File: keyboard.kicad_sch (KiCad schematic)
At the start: 207 parts, among them J2 USB_C_Receptacle_USB2.0_16P, J4 Conn_01x05, SW1 SW_Push, SW2 SW_Push, U1 RP2040, U2 XC6206PxxxMR, U3 W25Q128JVS, Y1 Crystal_GND24

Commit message: add logic level shifter to top sheet
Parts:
- added C101: 100n, symbol Device:C
- added R85: 470, symbol Device:R
- added U85: 74AHCT1G125, symbol 74xGxx:74AHCT1G125
- renumbered C16 to C100, C2 to C85, C3 to C86, C11 to C87, C10 to C88, C9 to C89, C8 to C90, C7 to C91, C6 to C92, C5 to C93, C4 to C94, C1 to C95, C12 to C96, C13 to C97, C15 to C98, C14 to C99, J2 to J1, J4 to J2, R8 to R1, R11 to R3, R1 to R4, R10 to R5, R9 to R6, R3 to R8, R6 to R9, S30 to S1, S59 to S2, S61 to S3, S78 to S4
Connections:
- net +5V: now also C101.1, U85.5 (VCC)
- net GND: now also C101.2, U85.1, U85.3 (GND)
- new net: R85.1, U85.4
- new net LED_DATA: R85.2, U85.2
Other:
- added sheet LED_link (LED_link_sch.kicad_sch)
- note added: "Logic Level Shifter"

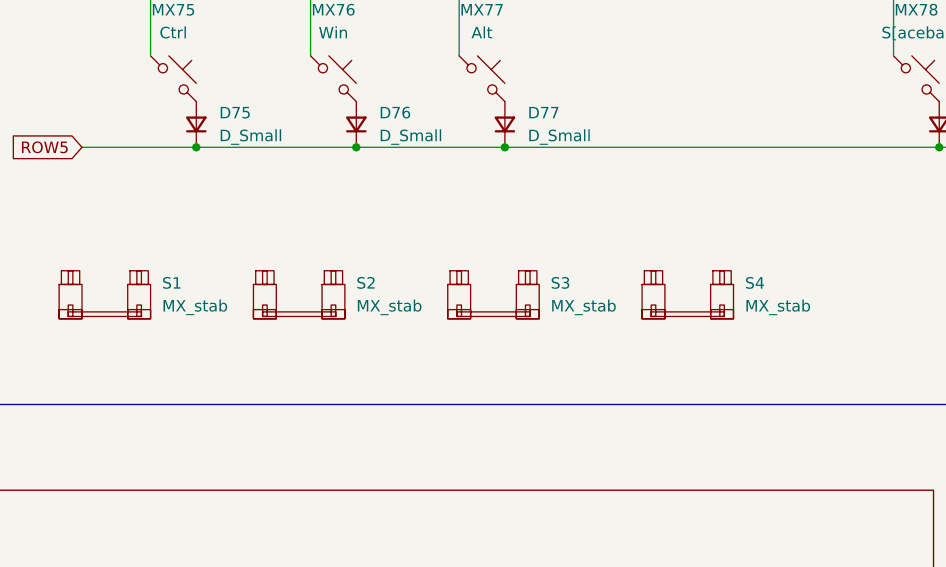
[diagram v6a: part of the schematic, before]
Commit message: flip mx switches, need to flip others as well
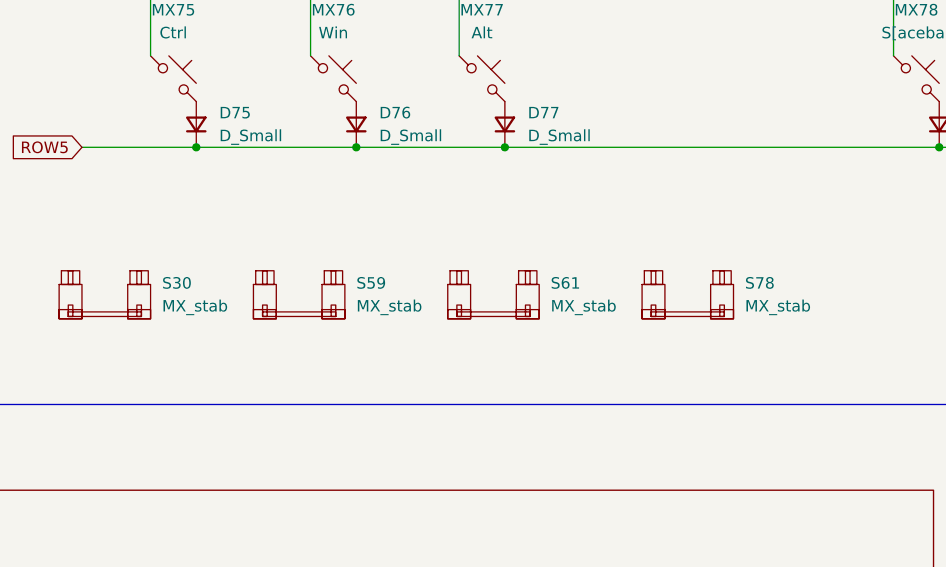
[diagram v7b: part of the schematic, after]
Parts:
- C100, C85, C86, C87, C88, C89, C90, C91, C92, C93, C94, C95, C98, C99: footprint Capacitor_SMD:C_0402_1005Metric -> Capacitor_SMD:C_0402_1005Metric_Pad0.74x0.62mm_HandSolder
- C101: footprint (none) -> Capacitor_SMD:C_0402_1005Metric_Pad0.74x0.62mm_HandSolder
- C96, C97: footprint Capacitor_SMD:C_0603_1608Metric -> Capacitor_SMD:C_0402_1005Metric_Pad0.74x0.62mm_HandSolder
- R85: footprint (none) -> Resistor_SMD:R_0402_1005Metric_Pad0.72x0.64mm_HandSolder
- U85: footprint (none) -> Package_TO_SOT_SMD:SOT-23-5_HandSoldering
- renumbered S1 to S30, S2 to S59, S3 to S61, S4 to S78
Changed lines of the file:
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@@
 			)
 		)
-		(property "Footprint" "Capacitor_SMD:C_0402_1005Metric"
+		(property "Footprint" "Capacitor_SMD:C_0402_1005Metric_Pad0.74x0.62mm_HandSolder"
 			(at 87.3252 34.29 0)
 			(hide yes)
@@
 		(dnp no)
 		(fields_autoplaced yes)
-		(property "Reference" "S4"
+		(property "Reference" "S78"
 			(at 323.85 162.4329 0)
 			(show_name no)
@@
 			(project "keyboard"
 				(path "/4d03a9a6-8b5c-48be-8b99-d5cd1aeff9bb"
-					(reference "S4")
+					(reference "S78")
 					(unit 1)
 				)
@@
 			)
 		)
-		(property "Footprint" "Capacitor_SMD:C_0603_1608Metric"
+		(property "Footprint" "Capacitor_SMD:C_0402_1005Metric_Pad0.74x0.62mm_HandSolder"
 			(at 88.5952 182.88 0)
 			(hide yes)
@@
 			)
 		)
-		(property "Footprint" "Capacitor_SMD:C_0402_1005Metric"
+		(property "Footprint" "Capacitor_SMD:C_0402_1005Metric_Pad0.74x0.62mm_HandSolder"
 			(at 149.5552 45.72 0)
 			(hide yes)
@@
 			)
 		)
-		(property "Footprint" ""
+		(property "Footprint" "Resistor_SMD:R_0402_1005Metric_Pad0.72x0.64mm_HandSolder"
 			(at 102.87 337.058 90)
 			(hide yes)
@@
 		(dnp no)
 		(fields_autoplaced yes)
-		(property "Reference" "S2"
+		(property "Reference" "S59"
 			(at 280.67 162.4329 0)
 			(show_name no)
@@
 			(project "keyboard"
 				(path "/4d03a9a6-8b5c-48be-8b99-d5cd1aeff9bb"
-					(reference "S2")
+					(reference "S59")
 					(unit 1)
 				)
@@
 			)
 		)
-		(property "Footprint" "Capacitor_SMD:C_0402_1005Metric"
+		(property "Footprint" "Capacitor_SMD:C_0402_1005Metric_Pad0.74x0.62mm_HandSolder"
 			(at 180.0352 241.3 0)
 			(hide yes)
@@
 			)
 		)
-		(property "Footprint" "Capacitor_SMD:C_0402_1005Metric"
+		(property "Footprint" "Capacitor_SMD:C_0402_1005Metric_Pad0.74x0.62mm_HandSolder"
 			(at 162.2552 33.02 0)
 			(hide yes)
@@
 			)
 		)
-		(property "Footprint" "Capacitor_SMD:C_0402_1005Metric"
+		(property "Footprint" "Capacitor_SMD:C_0402_1005Metric_Pad0.74x0.62mm_HandSolder"
 			(at 29.21 248.6152 0)
 			(hide yes)
@@
 		(dnp no)
 		(fields_autoplaced yes)
-		(property "Reference" "S1"
+		(property "Reference" "S30"
 			(at 259.08 162.4329 0)
 			(show_name no)
@@
 			(project "keyboard"
 				(path "/4d03a9a6-8b5c-48be-8b99-d5cd1aeff9bb"
-					(reference "S1")
+					(reference "S30")
 					(unit 1)
 				)
@@
 			)
 		)
-		(property "Footprint" "Capacitor_SMD:C_0402_1005Metric"
+		(property "Footprint" "Capacitor_SMD:C_0402_1005Metric_Pad0.74x0.62mm_HandSolder"
 			(at 149.5552 33.02 0)
 			(hide yes)
@@
 			)
 		)
-		(property "Footprint" "Capacitor_SMD:C_0603_1608Metric"
+		(property "Footprint" "Capacitor_SMD:C_0402_1005Metric_Pad0.74x0.62mm_HandSolder"
 			(at 125.4252 182.88 0)
 			(hide yes)
@@
 			)
 		)
-		(property "Footprint" ""
+		(property "Footprint" "Capacitor_SMD:C_0402_1005Metric_Pad0.74x0.62mm_HandSolder"
 			(at 41.6052 326.39 0)
 			(hide yes)
@@
 			)
 		)
-		(property "Footprint" "Capacitor_SMD:C_0402_1005Metric"
+		(property "Footprint" "Capacitor_SMD:C_0402_1005Metric_Pad0.74x0.62mm_HandSolder"
 			(at 61.9252 34.29 0)
 			(hide yes)
@@
 			)
 		)
-		(property "Footprint" "Capacitor_SMD:C_0402_1005Metric"
+		(property "Footprint" "Capacitor_SMD:C_0402_1005Metric_Pad0.74x0.62mm_HandSolder"
 			(at 49.2252 34.29 0)
 			(hide yes)
@@
 			)
 		)
-		(property "Footprint" "Capacitor_SMD:C_0402_1005Metric"
+		(property "Footprint" "Capacitor_SMD:C_0402_1005Metric_Pad0.74x0.62mm_HandSolder"
 			(at 35.2552 34.29 0)
 			(hide yes)
@@
 			)
 		)
-		(property "Footprint" "Capacitor_SMD:C_0402_1005Metric"
+		(property "Footprint" "Capacitor_SMD:C_0402_1005Metric_Pad0.74x0.62mm_HandSolder"
 			(at 36.83 233.9848 0)
 			(hide yes)
@@
 		(dnp no)
 		(fields_autoplaced yes)
-		(property "Reference" "S3"
+		(property "Reference" "S61"
 			(at 302.26 162.4329 0)
 			(show_name no)
@@
 			(project "keyboard"
 				(path "/4d03a9a6-8b5c-48be-8b99-d5cd1aeff9bb"
-					(reference "S3")
+					(reference "S61")
 					(unit 1)
 				)
@@
 			)
 		)
-		(property "Footprint" "Capacitor_SMD:C_0402_1005Metric"
+		(property "Footprint" "Capacitor_SMD:C_0402_1005Metric_Pad0.74x0.62mm_HandSolder"
 			(at 74.6252 34.29 0)
 			(hide yes)
@@
 			)
 		)
-		(property "Footprint" ""
+		(property "Footprint" "Package_TO_SOT_SMD:SOT-23-5_HandSoldering"
 			(at 72.39 335.28 0)
 			(hide yes)
@@
 			)
 		)
-		(property "Footprint" "Capacitor_SMD:C_0402_1005Metric"
+		(property "Footprint" "Capacitor_SMD:C_0402_1005Metric_Pad0.74x0.62mm_HandSolder"
 			(at 100.0252 45.72 0)
 			(hide yes)
@@
 			)
 		)
-		(property "Footprint" "Capacitor_SMD:C_0402_1005Metric"
+		(property "Footprint" "Capacitor_SMD:C_0402_1005Metric_Pad0.74x0.62mm_HandSolder"
 			(at 21.2852 34.29 0)
 			(hide yes)
@@
 			)
 		)
-		(property "Footprint" "Capacitor_SMD:C_0402_1005Metric"
+		(property "Footprint" "Capacitor_SMD:C_0402_1005Metric_Pad0.74x0.62mm_HandSolder"
 			(at 100.0252 34.29 0)
 			(hide yes)
